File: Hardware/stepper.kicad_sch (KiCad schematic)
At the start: 0 parts

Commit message: Completed schematic and PCB.
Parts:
- added A1, A2: Pololu_Breakout_DRV8825, Module:Pololu_Breakout-16_15.2x20.3mm, symbol Driver_Motor:Pololu_Breakout_DRV8825
- added C1, C2: 10u 25V, Capacitor_SMD:C_1206_3216Metric_Pad1.33x1.80mm_HandSolder, symbol Device:C_Small
- added J1, J2: DG250-3-5-04P-11-00AH, conn:DG250-3-5-04P-11-00AH, symbol Connector:Conn_01x04_Female
- added R1, R2, R3, R4: 10k, Resistor_SMD:R_0603_1608Metric_Pad0.98x0.95mm_HandSolder, symbol Device:R_Small
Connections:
- new net: A1.11 (M1), A2.11 (M1), R2.1
- new net: A1.12 (M2), A2.12 (M2), R1.1
- new net: A1.10 (M0), A2.10 (M0), R3.1
- new net: A1.14 (~{SLP}), A2.14 (~{SLP}), R4.1
- new net: A1.3 (A2), J1.2 (Pin_2)
- new net: A1.4 (A1), J1.1 (Pin_1)
- new net: A1.5 (B1), J1.3 (Pin_3)
- new net: A1.6 (B2), J1.4 (Pin_4)
- new net: A2.3 (A2), J2.2 (Pin_2)
- new net: A2.4 (A1), J2.1 (Pin_1)
- new net: A2.5 (B1), J2.3 (Pin_3)
- new net: A2.6 (B2), J2.4 (Pin_4)
- new net +15V: A1.8 (VMOT), A2.8 (VMOT), C1.2, C2.2
- new net EN: A1.9 (~{EN}), A2.9 (~{EN})
- new net FAULT: A1.2 (~{FLT}), A2.2 (~{FLT})
- new net GND: A1.1 (GND), A1.7 (GND), A2.1 (GND), A2.7 (GND), C1.1, C2.1
- new net RESET: A1.13 (~{RST}), A2.13 (~{RST})
- new net TEAR_DIR: A2.16 (DIR)
- new net TEAR_STEP: A2.15 (STEP)
- new net VDD: R1.2, R2.2, R3.2, R4.2
- new net Y_DIR: A1.16 (DIR)
- new net Y_STEP: A1.15 (STEP)

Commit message: Few coonector footprint modifications and silkscreen additions to them.
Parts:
- A1, A2: Link (none) -> https://ozdisan.com/maker-ve-iot-urunleri/arduino/arduino-m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; Price (none) -> 3.06830
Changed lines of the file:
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@@
+      (effects (font (size 1.27 1.27)) hide)
+    )
+    (property "Link" "https://ozdisan.com/maker-ve-iot-urunleri/arduino/arduino-modulleri/DRV8825-MOTOR-DRIVER" (id 4) (at 140.335 59.055 0)
+      (effects (font (size 1.27 1.27)) hide)
+    )
+    (property "Price" "3.06830" (id 5) (at 140.335 59.055 0)
       (effects (font (size 1.27 1.27)) hide)
     )
@@
       (effects (font (size 1.27 1.27)) hide)
     )
+    (property "Link" "https://ozdisan.com/maker-ve-iot-urunleri/arduino/arduino-modulleri/DRV8825-MOTOR-DRIVER" (id 4) (at 140.335 124.46 0)
+      (effects (font (size 1.27 1.27)) hide)
+    )
+    (property "Price" "3.06830" (id 5) (at 140.335 124.46 0)
+      (effects (font (size 1.27 1.27)) hide)
+    )

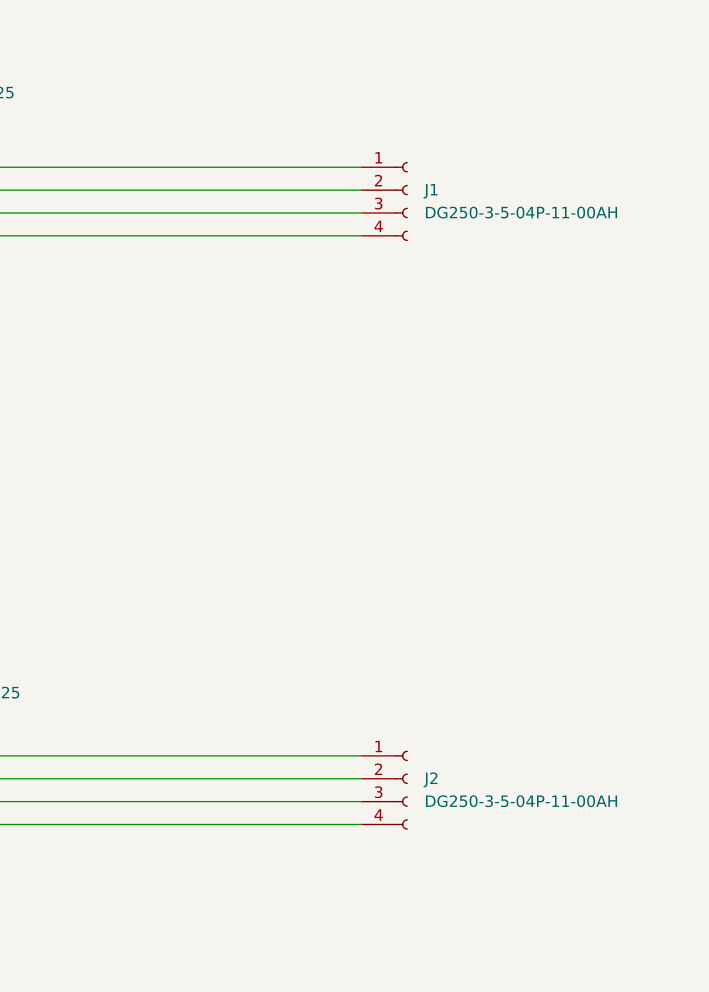
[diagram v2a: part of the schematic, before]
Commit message: Toolchain set. Timer module added. Schematic files migrated.
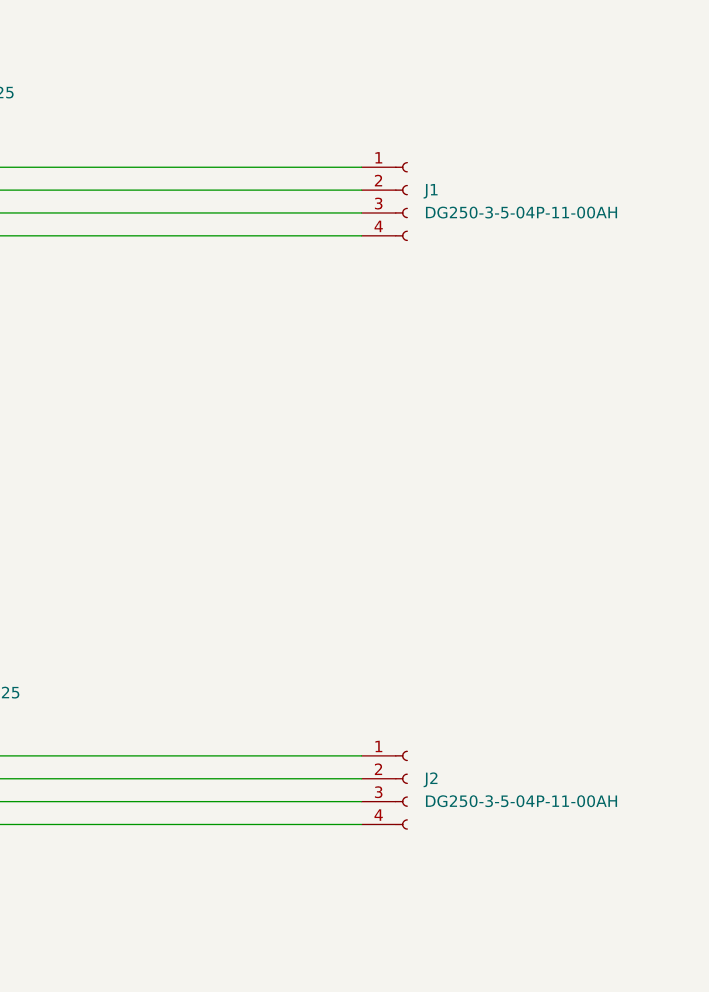
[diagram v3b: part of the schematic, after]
